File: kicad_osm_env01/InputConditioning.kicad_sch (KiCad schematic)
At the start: 0 parts

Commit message: updated mod list
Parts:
- added C? (x6): 100nF, Capacitor_SMD:C_0603_1608Metric, symbol LoTI_Board-rescue:C-device
- added R? (x4): 330R, Resistor_SMD:R_0603_1608Metric, symbol LoTI_Board-rescue:R-device
- added R? (x4): 100R, Resistor_SMD:R_0603_1608Metric, symbol LoTI_Board-rescue:R-device
- added R? (x4): DNF, Resistor_SMD:R_0603_1608Metric, symbol LoTI_Board-rescue:R-device
- added U? (x4): AD8646, Package_SO:SOIC-8_3.9x4.9mm_P1.27mm, symbol LoTI_Board-rescue:OPA2340-linear
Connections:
- new net: R?.1, R?.2, U?.5 (+) (x2)
- new net: R?.2, U?.6 (-), U?.7 (x2)
- new net: R?.1, R?.2, U?.3 (+) (x2)
- new net: R?.2, U?.1, U?.2 (-) (x2)
- new net +3V3: C?.2, C?.2, U?.8 (V+), U?.8 (V+)
- new net 3V3_ADC_CH1: C?.2, R?.1
- new net 3V3_ADC_CH2: C?.2, R?.1
- new net 3V3_ADC_CH3: C?.2, R?.1
- new net 3V3_ADC_CH4: C?.2, R?.1
- new net 3V3_SENSE1: R?.2
- new net 3V3_SENSE2: R?.2
- new net 3V3_SENSE3: R?.2
- new net 3V3_SENSE4: R?.2
- new net GND: C?.1, C?.1, C?.1, C?.1, C?.1, C?.1, R?.1, R?.1, R?.1, R?.1, U?.4 (V-), U?.4 (V-)

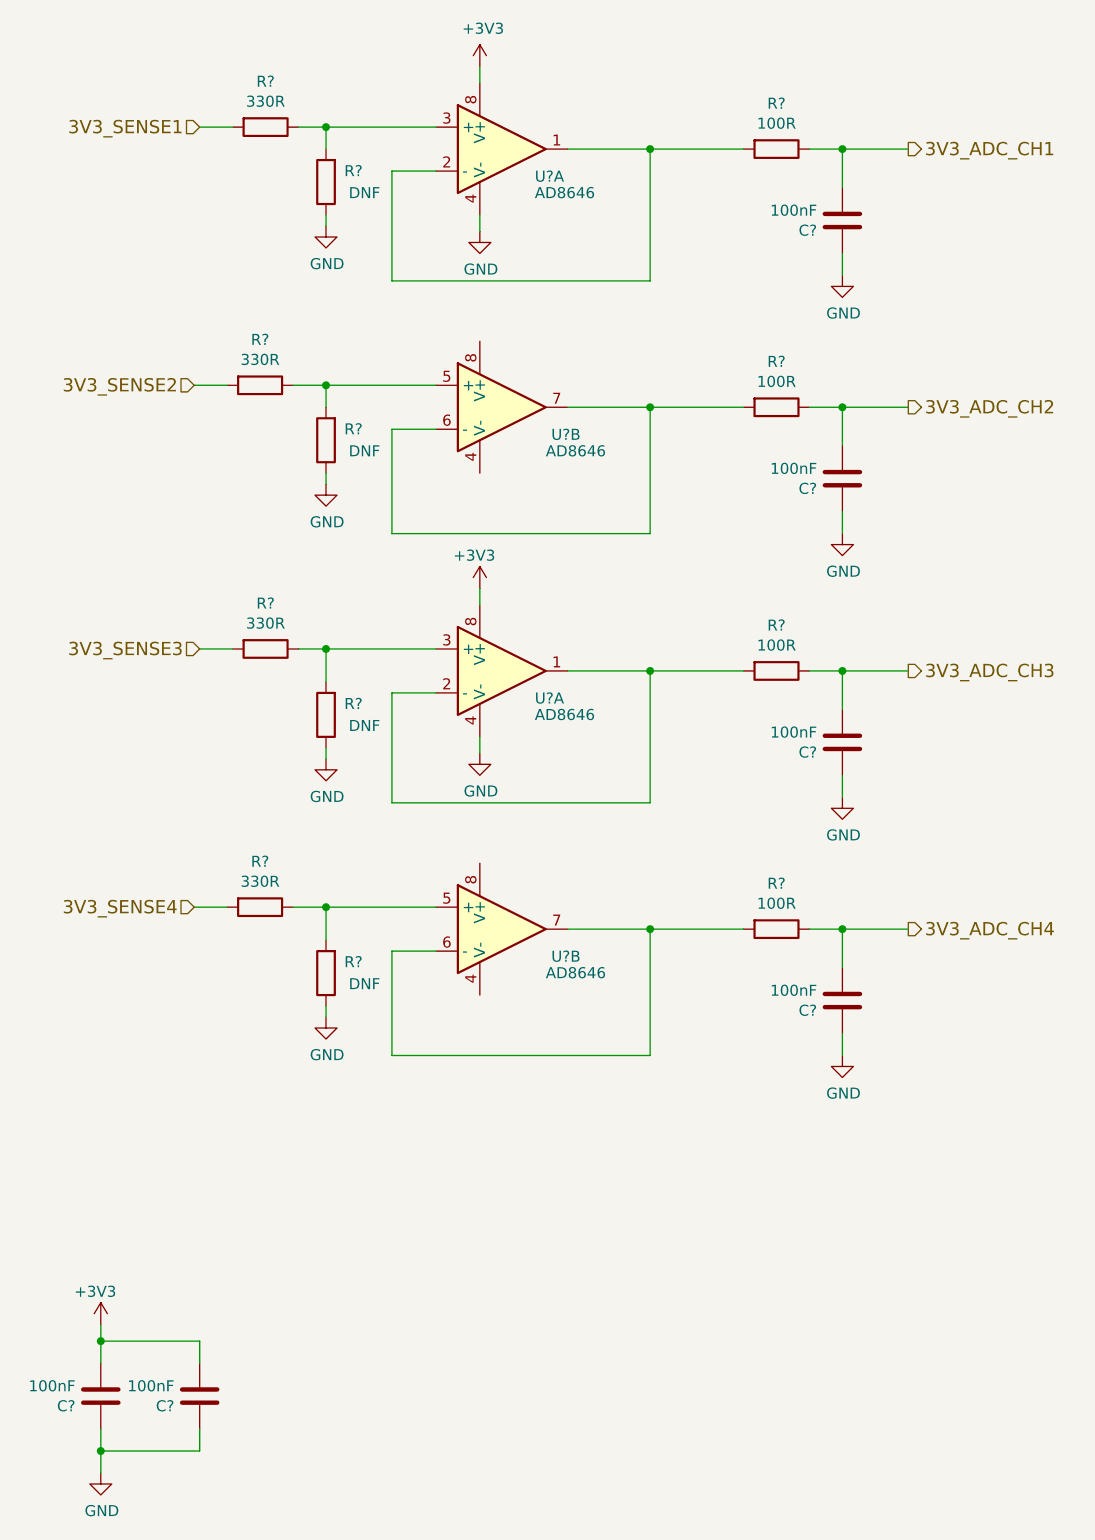
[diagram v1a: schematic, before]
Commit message: added new battery charge ic u2
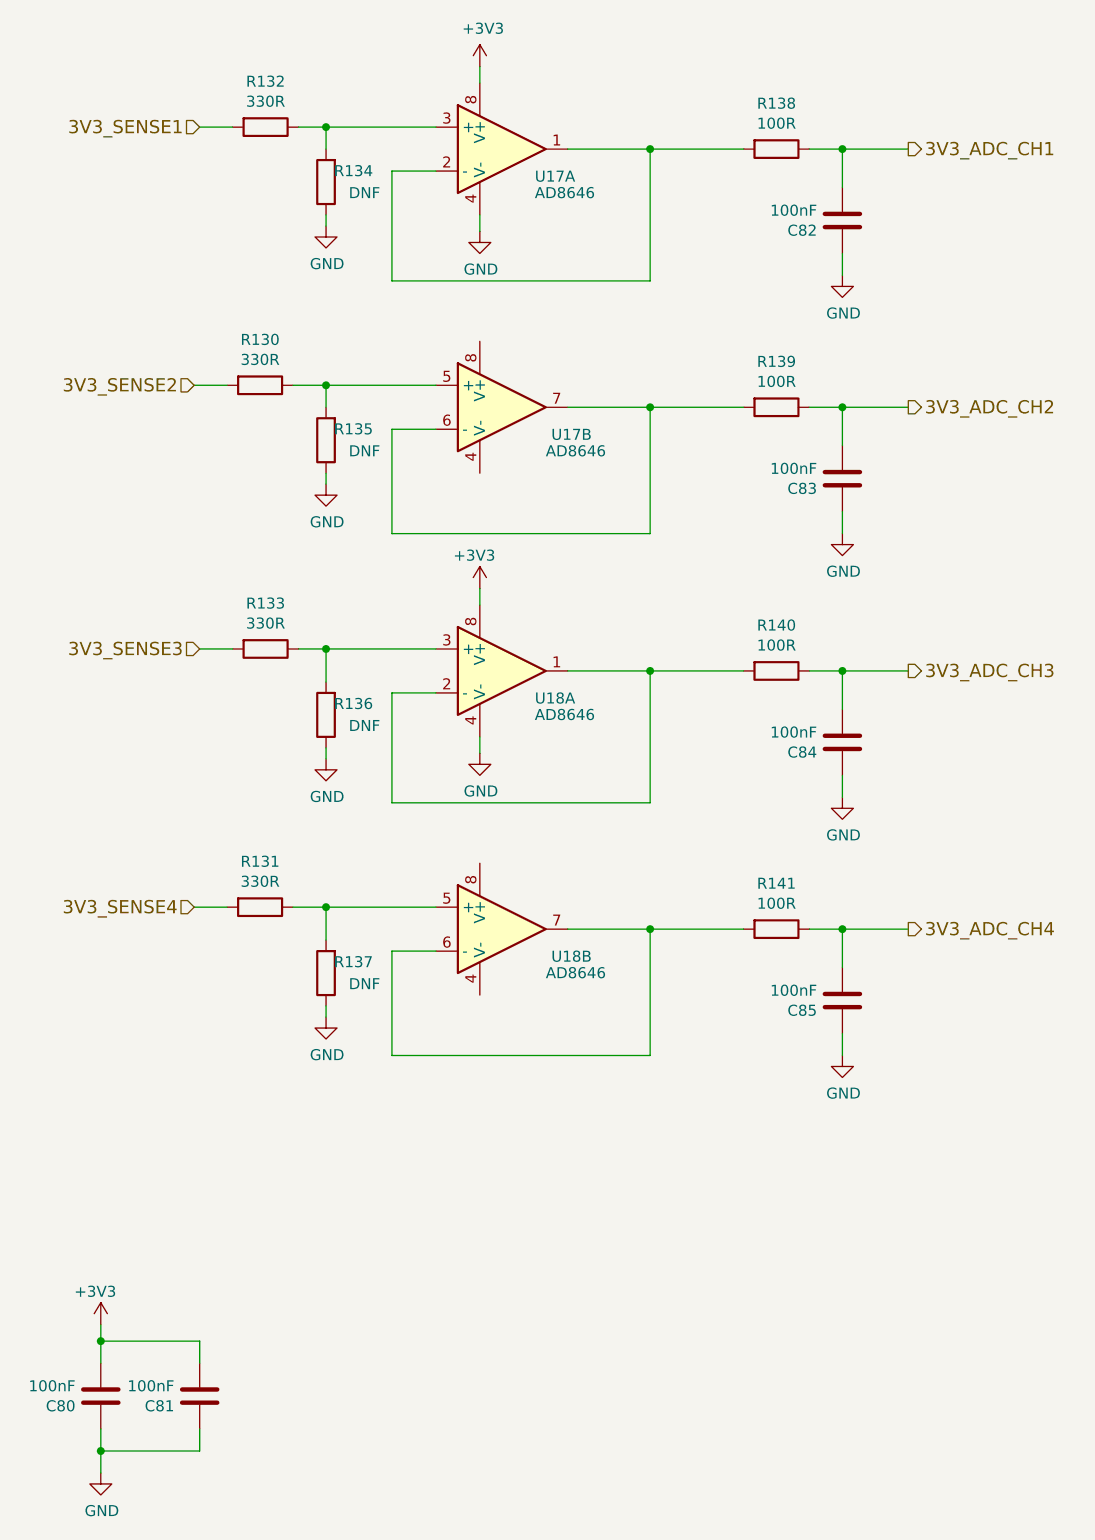
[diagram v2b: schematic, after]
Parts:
- gave numbers to parts that had none: 20
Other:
- company: (none) -> Devtank LTD
- title: (none) -> Open Smart Monitor
